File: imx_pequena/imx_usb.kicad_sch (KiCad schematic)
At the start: 16 parts, among them J4 USB_C_Receptacle, J5 USB_A

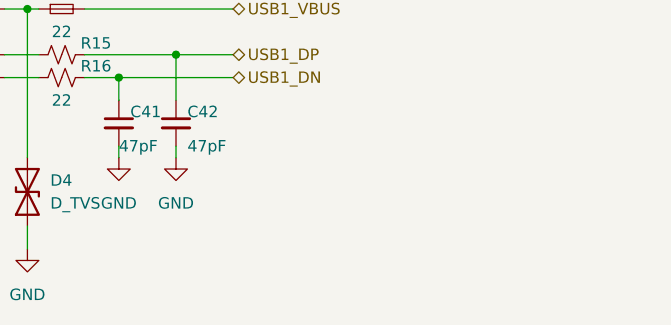
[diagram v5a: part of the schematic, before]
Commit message: fixed part alllocation
fixed socket to pin header issue
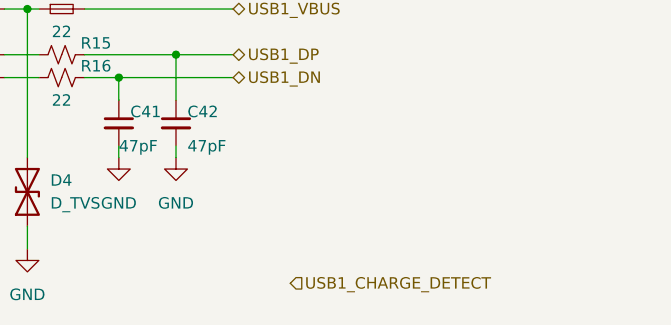
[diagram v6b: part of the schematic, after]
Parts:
- J4: footprint (none) -> Connector_USB:USB_C_Receptacle_Amphenol_12401610E4-2A_CircularHoles
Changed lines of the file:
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@@
+    (effects (font (size 1.27 1.27)) (justify left))
+  )
+  (hierarchical_label "USB1_CHARGE_DETECT" (shape input) (at 63.5 142.24 0)
     (effects (font (size 1.27 1.27)) (justify left))
   )
@@
     (property "Reference" "J4" (id 0) (at 29.21 17.78 0))
     (property "Value" "USB_C_Receptacle" (id 1) (at 29.21 20.32 0))
-    (property "Footprint" "" (id 2) (at 33.02 50.8 0)
-      (effects (font (size 1.27 1.27)) hide)
-    )
+    (property "Footprint" "Connector_USB:USB_C_Receptacle_Amphenol_12401610E4-2A_CircularHoles" (id 2) (at 33.02 50.8 0)
+      (effects (font (size 1.27 1.27)) hide)
+    )
